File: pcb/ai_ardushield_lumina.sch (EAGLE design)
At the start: 90 parts, among them J1 1X02ST, J2 1X01, J3 1X06, J4 1X08, J5 1X08, J6 1X10, U1 ARDUINOUNOR3-STRAIGHT

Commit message: Modified the routing quite a bit.
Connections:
- removed net N$47: LED8.VSS
- net GND: now also C38.2, LED8.VSS
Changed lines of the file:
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@@
 <setting verticaltext="up"/>
 </settings>
-<grid distance="0.1" unitdist="inch" unit="inch" style="lines" multiple="1" display="no" altdistance="0.01" altunitdist="inch" altunit="inch"/>
+<grid distance="50" unitdist="mil" unit="mil" style="lines" multiple="1" display="yes" altdistance="0.01" altunitdist="inch" altunit="inch"/>
 <layers>
 <layer number="1" name="Top" color="4" fill="1" visible="no" active="no"/>
@@
 <layer number="111" name="LPC17xx" color="7" fill="1" visible="yes" active="yes"/>
 <layer number="112" name="tSilk" color="7" fill="1" visible="yes" active="yes"/>
+<layer number="113" name="Route13" color="7" fill="1" visible="no" active="no"/>
 <layer number="116" name="Patch_BOT" color="9" fill="4" visible="no" active="yes"/>
+<layer number="117" name="mPads" color="7" fill="1" visible="no" active="no"/>
+<layer number="118" name="mVias" color="7" fill="1" visible="no" active="no"/>
+<layer number="119" name="mUnrouted" color="7" fill="1" visible="no" active="no"/>
+<layer number="120" name="mDimension" color="7" fill="1" visible="no" active="no"/>
 <layer number="121" name="_tsilk" color="7" fill="1" visible="no" active="yes"/>
 <layer number="122" name="_bsilk" color="7" fill="1" visible="no" active="yes"/>
@@
 <layer number="127" name="_tValues" color="7" fill="1" visible="yes" active="yes"/>
 <layer number="128" name="_bValues" color="7" fill="1" visible="yes" active="yes"/>
+<layer number="129" name="mtStop" color="7" fill="1" visible="no" active="no"/>
+<layer number="130" name="mbStop" color="7" fill="1" visible="no" active="no"/>
 <layer number="131" name="tAdjust" color="7" fill="1" visible="no" active="yes"/>
 <layer number="132" name="bAdjust" color="7" fill="1" visible="no" active="yes"/>
+<layer number="133" name="mtFinish" color="7" fill="1" visible="no" active="no"/>
+<layer number="134" name="mbFinish" color="7" fill="1" visible="no" active="no"/>
+<layer number="135" name="mtGlue" color="7" fill="1" visible="no" active="no"/>
+<layer number="136" name="mbGlue" color="7" fill="1" visible="no" active="no"/>
+<layer number="137" name="mtTest" color="7" fill="1" visible="no" active="no"/>
+<layer number="138" name="mbTest" color="7" fill="1" visible="no" active="no"/>
+<layer number="139" name="mtKeepout" color="7" fill="1" visible="no" active="no"/>
+<layer number="140" name="mbKeepout" color="7" fill="1" visible="no" active="no"/>
+<layer number="141" name="mtRestrict" color="7" fill="1" visible="no" active="no"/>
+<layer number="142" name="mbRestrict" color="7" fill="1" visible="no" active="no"/>
+<layer number="143" name="mvRestrict" color="7" fill="1" visible="no" active="no"/>
 <layer number="144" name="Drill_legend" color="7" fill="1" visible="no" active="yes"/>
+<layer number="145" name="mHoles" color="7" fill="1" visible="no" active="no"/>
+<layer number="146" name="mMilling" color="7" fill="1" visible="no" active="no"/>
+<layer number="147" name="mMeasures" color="7" fill="1" visible="no" active="no"/>
+<layer number="148" name="mDocument" color="7" fill="1" visible="no" active="no"/>
+<layer number="149" name="mReference" color="7" fill="1" visible="no" active="no"/>
 <layer number="150" name="Notes" color="7" fill="1" visible="no" active="yes"/>
 <layer number="151" name="HeatSink" color="7" fill="1" visible="no" active="yes"/>
@@
 <layer number="154" name="FabDoc2" color="2" fill="1" visible="no" active="no"/>
 <layer number="155" name="FabDoc3" color="7" fill="15" visible="no" active="no"/>
+<layer number="191" name="mNets" color="7" fill="1" visible="no" active="no"/>
+<layer number="192" name="mBusses" color="7" fill="1" visible="no" active="no"/>
+<layer number="193" name="mPins" color="7" fill="1" visible="no" active="no"/>
+<layer number="194" name="mSymbols" color="7" fill="1" visible="no" active="no"/>
+<layer number="195" name="mNames" color="7" fill="1" visible="no" active="no"/>
+<layer number="196" name="mValues" color="7" fill="1" visible="no" active="no"/>
 <layer number="199" name="Contour" color="7" fill="1" visible="no" active="yes"/>
 <layer number="200" name="200bmp" color="1" fill="10" visible="no" active="yes"/>
@@
 <part name="FRAME1" library="Ai_Miscellany" deviceset="FRAME-LETTER" device="">
 <attribute name="AUTHOR" value="A.I. HARDWARE SITH LORDS"/>
-<attribute name="REV" value="1.0"/>
+<attribute name="REV" value="1.1"/>
 </part>
 <part name="U1" library="Ai_Boards" deviceset="ARDUINO" device="UNOR3-STRAIGHT" value="ARDUINOUNOR3-STRAIGHT"/>
@@
 <instance part="GND5" gate="GND" x="24.13" y="12.7"/>
 <instance part="U$6" gate="G$1" x="10.16" y="170.18"/>
-<instance part="U$7" gate="G$1" x="36.83" y="22.86"/>
+<instance part="U$7" gate="G$1" x="35.56" y="22.86"/>
 <instance part="U$8" gate="1" x="30.48" y="22.86" smashed="yes"/>
 <instance part="J3" gate="M06X1" x="3.81" y="137.16"/>
@@
 <wire x1="134.62" y1="151.13" x2="137.16" y2="151.13" width="0.1524" layer="91"/>
 <junction x="137.16" y="151.13"/>
-<wire x1="133.35" y1="62.23" x2="134.62" y2="62.23" width="0.1524" layer="91"/>
-<junction x="137.16" y="62.23"/>
 <pinref part="LED9" gate="U1" pin="VSS"/>
-<wire x1="134.62" y1="62.23" x2="137.16" y2="62.23" width="0.1524" layer="91"/>
 <wire x1="134.62" y1="44.45" x2="137.16" y2="44.45" width="0.1524" layer="91"/>
 <junction x="137.16" y="44.45"/>
@@
 <junction x="137.16" y="128.27"/>
 <pinref part="LED10" gate="U1" pin="VSS"/>
-<junction x="134.62" y="62.23"/>
+<wire x1="134.62" y1="62.23" x2="137.16" y2="62.23" width="0.1524" layer="91"/>
+<junction x="137.16" y="62.23"/>
 </segment>
 <segment>
@@
 <wire x1="64.77" y1="90.17" x2="64.77" y2="72.39" width="0.1524" layer="91"/>
 <wire x1="64.77" y1="72.39" x2="64.77" y2="54.61" width="0.1524" layer="91"/>
-<wire x1="64.77" y1="54.61" x2="64.77" y2="29.21" width="0.1524" layer="91"/>
+<wire x1="64.77" y1="54.61" x2="64.77" y2="36.83" width="0.1524" layer="91"/>
+<wire x1="64.77" y1="36.83" x2="64.77" y2="29.21" width="0.1524" layer="91"/>
 <wire x1="69.85" y1="54.61" x2="64.77" y2="54.61" width="0.1524" layer="91"/>
 <junction x="64.77" y="54.61"/>
@@
 <wire x1="69.85" y1="143.51" x2="64.77" y2="143.51" width="0.1524" layer="91"/>
 <junction x="64.77" y="143.51"/>
+<pinref part="LED8" gate="U1" pin="VSS"/>
+<wire x1="69.85" y1="36.83" x2="64.77" y2="36.83" width="0.1524" layer="91"/>
+<junction x="64.77" y="36.83"/>
 </segment>
 <segment>
@@
 <wire x1="207.01" y1="151.13" x2="209.55" y2="151.13" width="0.1524" layer="91"/>
 <junction x="209.55" y="151.13"/>
-<wire x1="205.74" y1="62.23" x2="207.01" y2="62.23" width="0.1524" layer="91"/>
-<junction x="209.55" y="62.23"/>
-<wire x1="207.01" y1="62.23" x2="209.55" y2="62.23" width="0.1524" layer="91"/>
 <wire x1="207.01" y1="44.45" x2="209.55" y2="44.45" width="0.1524" layer="91"/>
 <junction x="209.55" y="44.45"/>
 <pinref part="LED25" gate="U1" pin="VSS"/>
-<pinref part="LED26" gate="U1" pin="VSS"/>
-<junction x="207.01" y="62.23"/>
 <pinref part="LED27" gate="U1" pin="VSS"/>
 <pinref part="LED28" gate="U1" pin="VSS"/>
@@
 <wire x1="214.63" y1="146.05" x2="209.55" y2="146.05" width="0.1524" layer="91"/>
 <junction x="209.55" y="146.05"/>
+<pinref part="LED26" gate="U1" pin="VSS"/>
+<wire x1="207.01" y1="62.23" x2="209.55" y2="62.23" width="0.1524" layer="91"/>
+<junction x="209.55" y="62.23"/>
 </segment>
 <segment>
@@
 <wire x1="26.67" y1="41.91" x2="33.02" y2="41.91" width="0.1524" layer="91"/>
 <wire x1="33.02" y1="41.91" x2="36.83" y2="41.91" width="0.1524" layer="91"/>
-<wire x1="36.83" y1="41.91" x2="46.99" y2="41.91" width="0.1524" layer="91"/>
+<wire x1="36.83" y1="41.91" x2="40.64" y2="41.91" width="0.1524" layer="91"/>
+<wire x1="40.64" y1="41.91" x2="46.99" y2="41.91" width="0.1524" layer="91"/>
 <wire x1="46.99" y1="41.91" x2="53.34" y2="41.91" width="0.1524" layer="91"/>
 <wire x1="53.34" y1="41.91" x2="53.34" y2="43.18" width="0.1524" layer="91"/>
@@
 <junction x="12.7" y="102.87"/>
 <junction x="36.83" y="102.87"/>
+<pinref part="C38" gate="G$1" pin="2"/>
+<wire x1="40.64" y1="43.18" x2="40.64" y2="41.91" width="0.1524" layer="91"/>
+<junction x="40.64" y="41.91"/>
 </segment>
 <segment>
@@
 </segment>
 </net>
-<net name="N$47" class="0">
-<segment>
-<pinref part="LED8" gate="U1" pin="VSS"/>
-<wire x1="69.85" y1="36.83" x2="64.77" y2="36.83" width="0.1524" layer="91"/>
-</segment>
-</net>
 <net name="VLED" class="0">
 <segment>
@@
 <segment>
 <pinref part="JP1" gate="G$1" pin="1"/>
-<wire x1="20.32" y1="3.81" x2="36.83" y2="3.81" width="0.1524" layer="91"/>
-<wire x1="36.83" y1="3.81" x2="36.83" y2="22.86" width="0.1524" layer="91"/>
+<wire x1="20.32" y1="3.81" x2="35.56" y2="3.81" width="0.1524" layer="91"/>
+<wire x1="35.56" y1="3.81" x2="35.56" y2="22.86" width="0.1524" layer="91"/>
 <pinref part="U$7" gate="G$1" pin="5V"/>
 </segment>
@@
 <pinref part="J6" gate="M10X1" pin="10"/>
 <wire x1="54.61" y1="152.4" x2="52.07" y2="152.4" width="0.1524" layer="91"/>
-<label x="48.26" y="152.4" size="1.778" layer="95" ratio="15"/>
+<label x="48.26" y="152.4" size="1.524" layer="95" ratio="15"/>
 </segment>
 <segment>
 <pinref part="LED1" gate="U1" pin="DI"/>
 <wire x1="97.79" y1="168.91" x2="100.33" y2="168.91" width="0.1524" layer="91"/>
-<label x="96.52" y="168.91" size="1.778" layer="95" ratio="15"/>
+<label x="100.33" y="173.99" size="1.27" layer="95" ratio="15" rot="R90" xref="yes"/>
+<wire x1="100.33" y1="173.99" x2="100.33" y2="168.91" width="0.1524" layer="91"/>
 </segment>
 </net>
@@
 <pinref part="U1" gate="G$1" pin="RESET"/>
 <wire x1="8.89" y1="160.02" x2="11.43" y2="160.02" width="0.1524" layer="91"/>
-<label x="11.43" y="160.02" size="1.778" layer="95" ratio="15"/>
-</segment>
-</net>
+<label x="11.43" y="160.02" size="1.524" layer="95" ratio="15"/>
+</segment>
+</net>

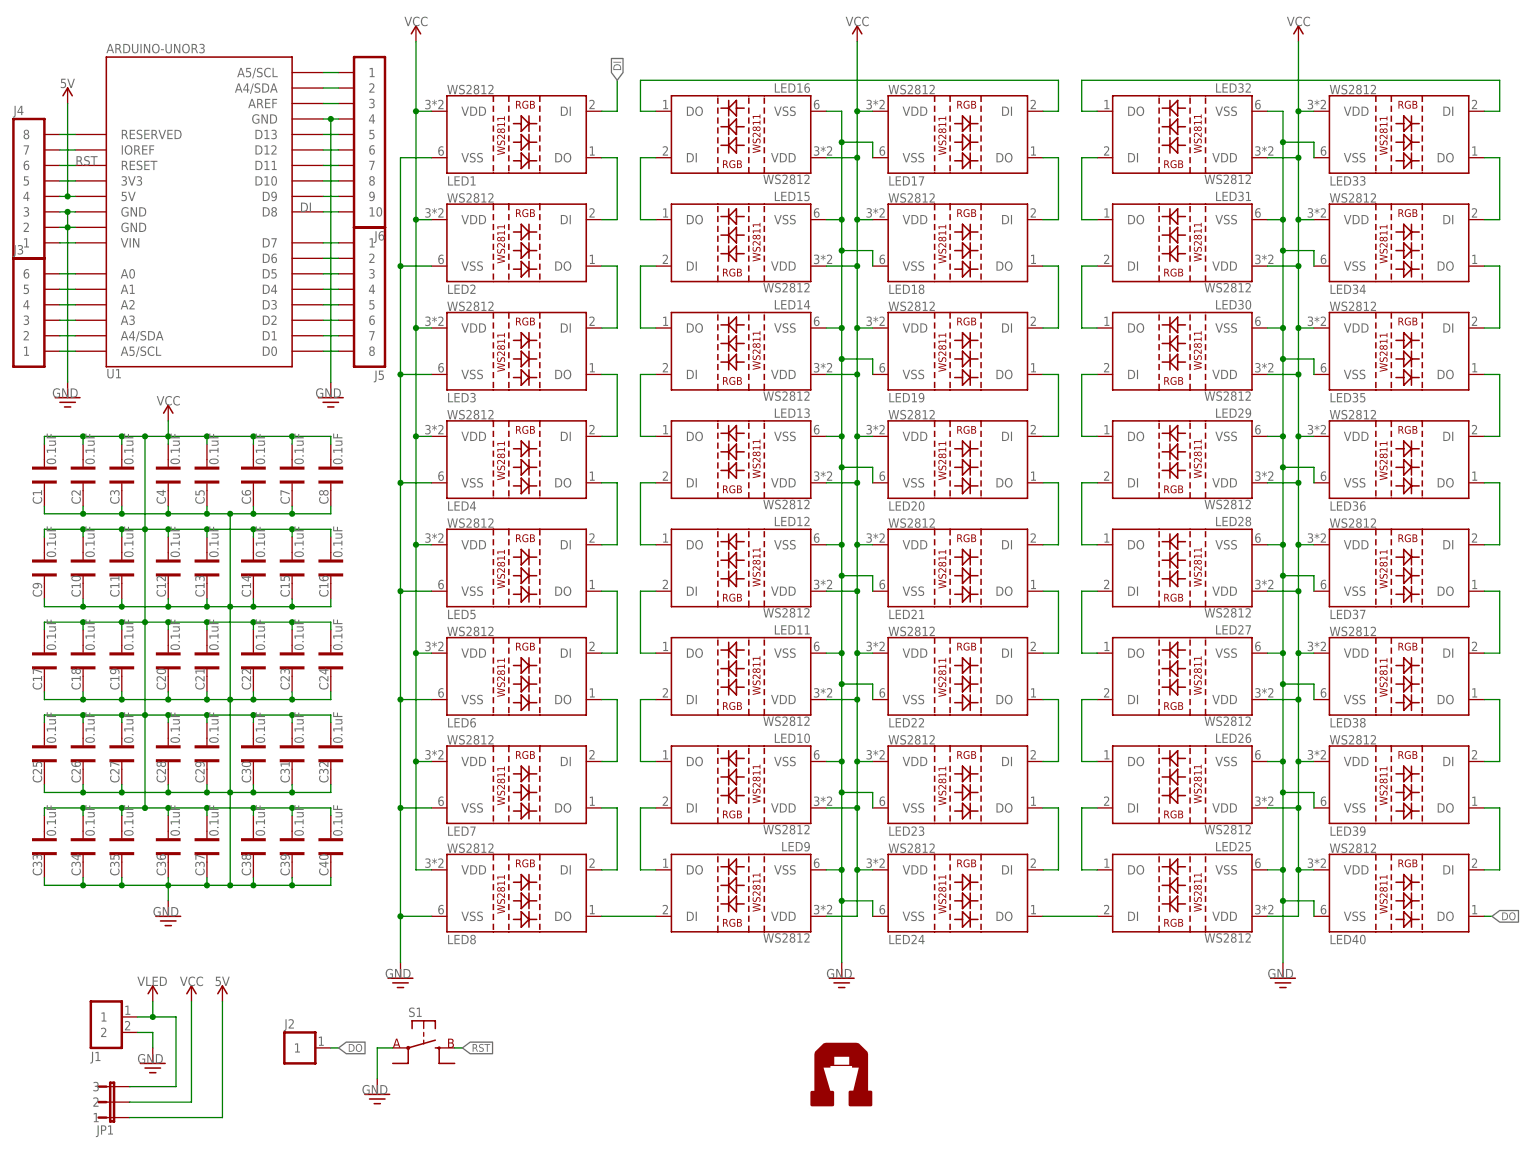
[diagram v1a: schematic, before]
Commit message: Changed design to use WS2812Bs
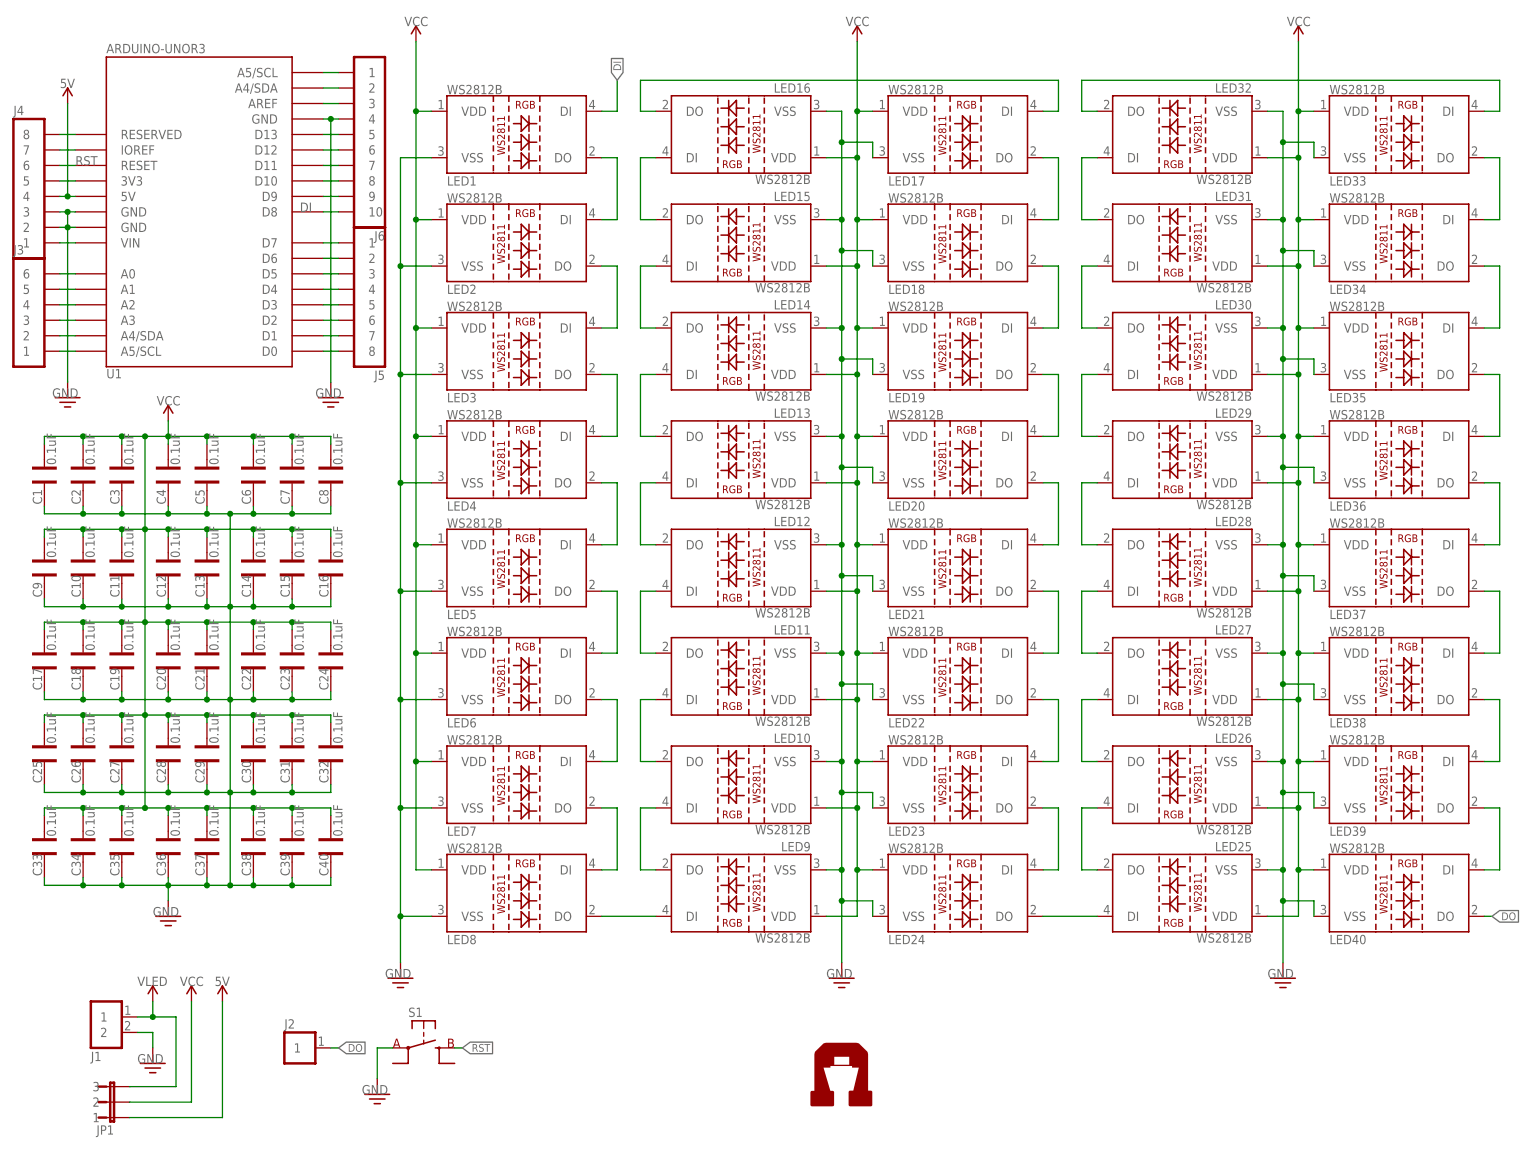
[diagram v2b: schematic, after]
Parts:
- LED1, LED10, LED11, LED12, LED13, LED14, LED15, LED16, LED17, LED18, LED19, LED2, LED20, LED21, LED22, LED23, LED24, LED25, LED26, LED27, LED28, LED29, LED3, LED30, LED31, LED32, LED33, LED34, LED35, LED36, LED37, LED38, LED39, LED4, LED40, LED5, LED6, LED7, LED8, LED9: value LED-WS2812 -> LED-WS2812B; device Ai_LED:LED-WS2812 -> Ai_LED:LED-WS2812B
